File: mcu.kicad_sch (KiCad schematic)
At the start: 7 parts, among them SW1 Reset Switch, U2 STM32F030F4Px

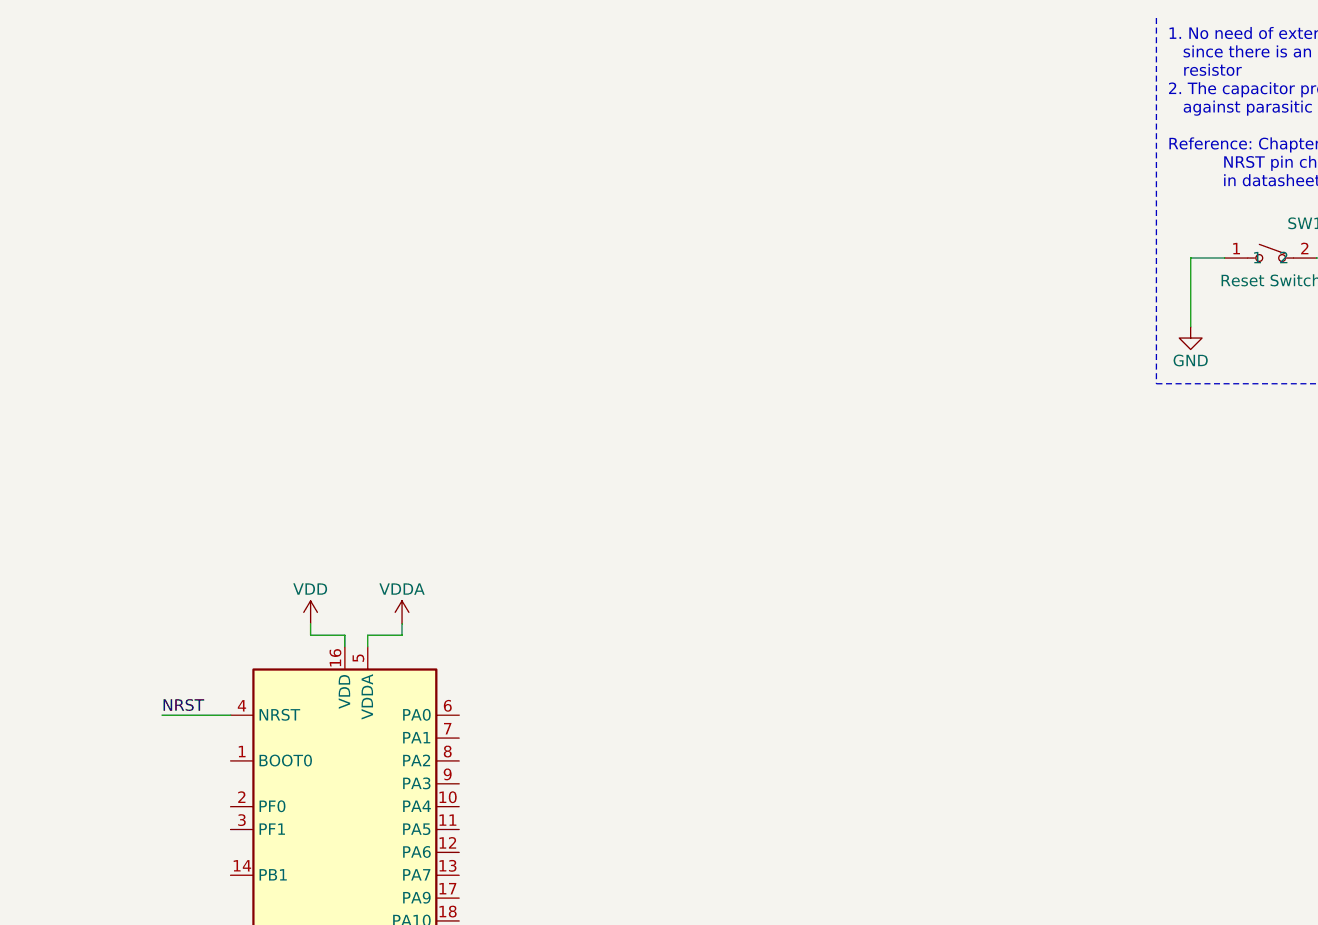
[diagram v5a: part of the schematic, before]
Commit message: feat(boot_mode): Add boot mode selection circuit for MCU BOOT0 pin
Implements the boot mode selection circuitry for the microcontroller's BOOT0 pin in the schematic.

This includes:
- Placement of selection components (e.g., jumper, switch, resistors).
- Configuration to allow selection of different boot modes.
- Connection to the MCU's BOOT0 pin.

This addition provides flexibility in configuring the microcontroller's boot process for tasks such as programming or normal operation.
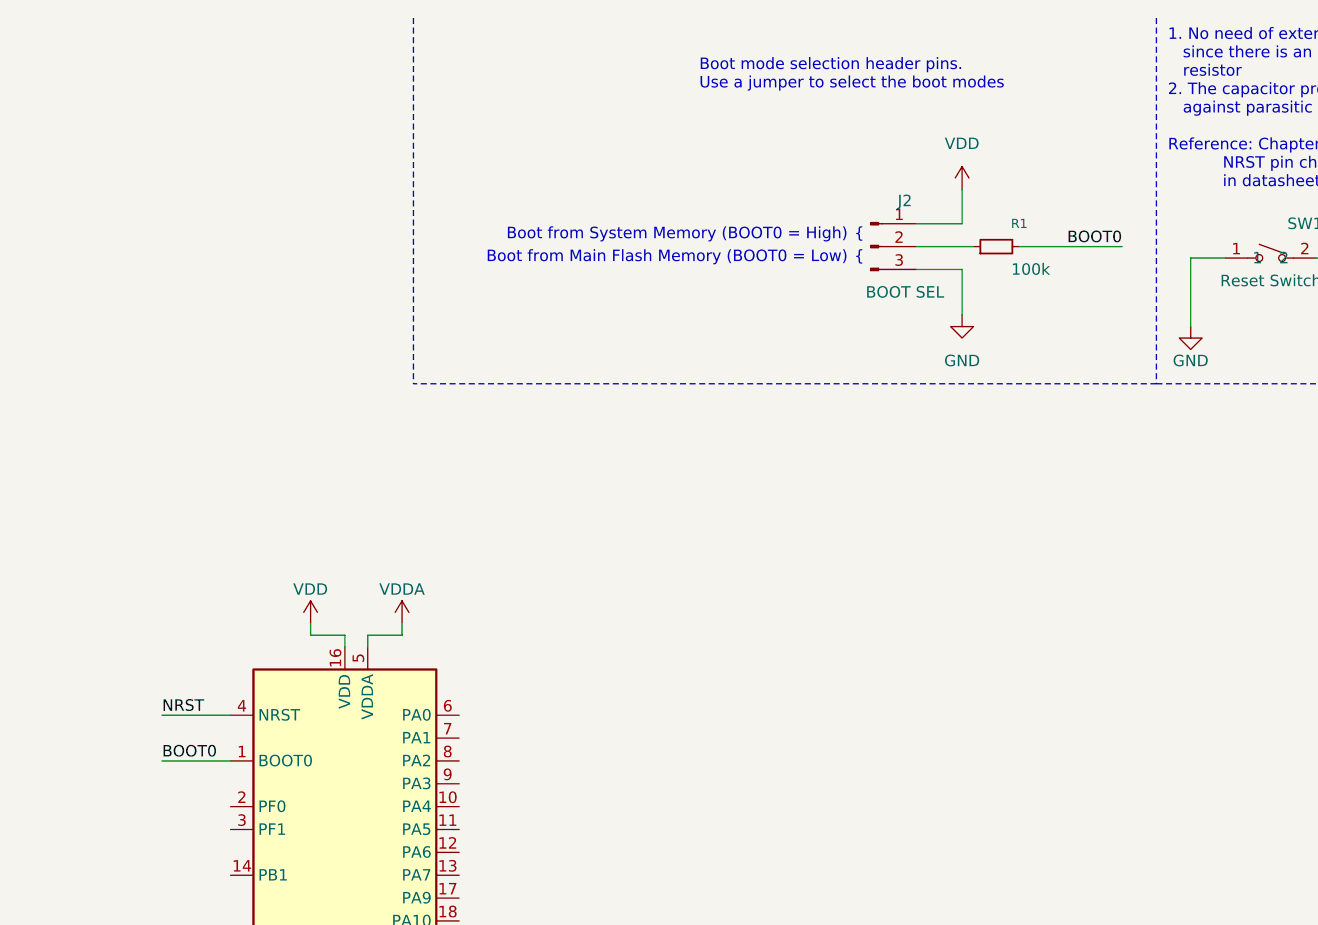
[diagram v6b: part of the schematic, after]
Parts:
- added J2: BOOT SEL, symbol Connector:Conn_01x03_Pin
- added R1: 100k, Resistor_SMD:R_0201_0603Metric_Pad0.64x0.40mm_HandSolder, symbol Device:R_Small
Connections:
- net GND: now also J2.3 (Pin_3)
- net VDD: now also J2.1 (Pin_1)
- net BOOT0: now reaches U2.1 (BOOT0)
- net BOOT0: now also R1.2
- new net: J2.2 (Pin_2), R1.1
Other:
- note added: "Boot from Main Flash Memory (BOOT0 = Low)"
- note added: "Boot from System Memory (BOOT0 = High)"
- note added: "Boot mode selection header pins. Use a jumper to select the boot modes"
- note added: "{"

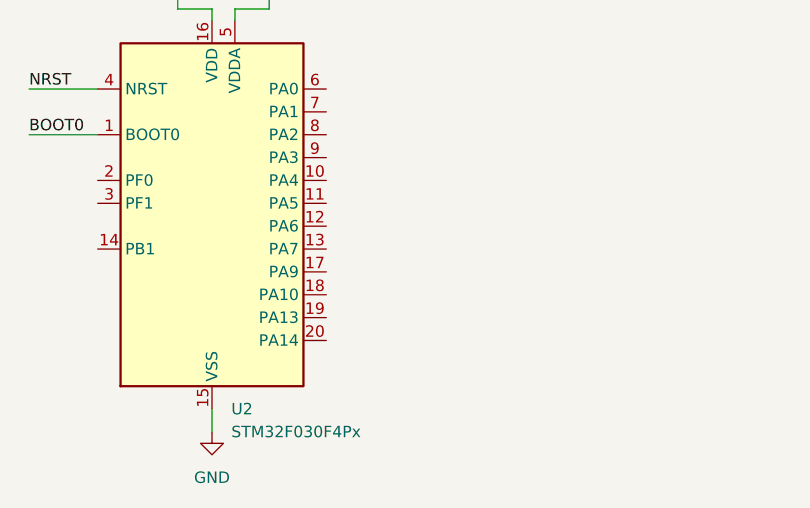
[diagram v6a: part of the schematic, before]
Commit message: feat(usb-uart): add FT232RL USB‑UART bridge and wire RX/TX to MCU
Added the FT232RL USB‑to‑UART interface IC (FT232RL) into the schematic and powered it from the 3.3 V and 5 V rails. Exposed its TTL-level RXD and TXD pins through the hierarchical sheet and connected it to the MCU

- Placed FT232RL SSOP‑28 symbol and footprint, tied VCCIO to 3.3 V, VCC to USB_VCC, and GND to ground.
- Left legacy RS‑232 control lines (DSR#, DCD#, RI#) and CBUS pins unconnected.
- Updated hierarchy:added sheet pins on USB_UART page.

This enables USB‑serial communication between host PC and STM32F030F4Px
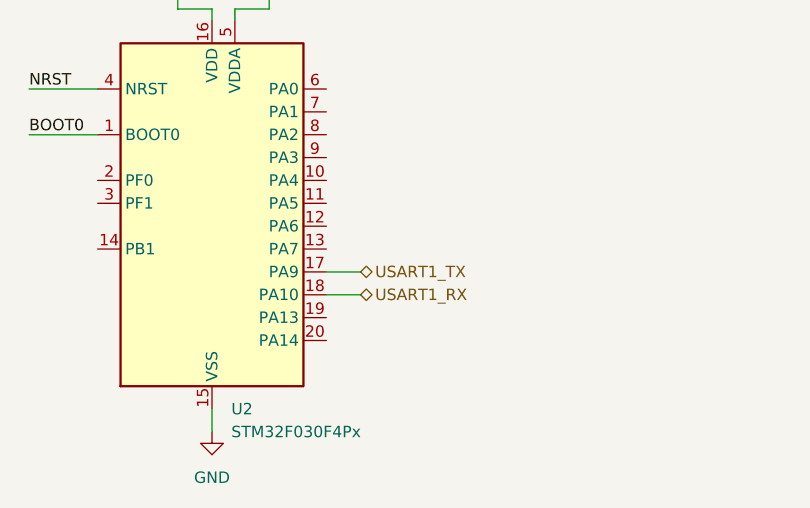
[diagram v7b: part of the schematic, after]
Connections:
- net USART1_TX: now reaches U2.17 (PA9)
- net USART1_RX: now reaches U2.18 (PA10)
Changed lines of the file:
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@@
 		(color 0 0 0 0)
 	)
+	(wire
+		(pts
+			(xy 167.64 110.49) (xy 171.45 110.49)
+		)
+		(stroke
+			(width 0)
+			(type default)
+		)
+	)
 	(polyline
 		(pts
@@
 		(pts
 			(xy 134.62 95.25) (xy 142.24 95.25)
+		)
+		(stroke
+			(width 0)
+			(type default)
+		)
+	)
+	(wire
+		(pts
+			(xy 167.64 113.03) (xy 171.45 113.03)
 		)
 		(stroke
@@
 			)
 			(justify right bottom)
+		)
+	)
+	(hierarchical_label "USART1_TX"
+		(shape bidirectional)
+		(at 171.45 110.49 0)
+		(effects
+			(font
+				(size 1.27 1.27)
+			)
+			(justify left)
 		)
 	)
@@
 		)
 	)
+	(hierarchical_label "USART1_RX"
+		(shape bidirectional)
+		(at 171.45 113.03 0)
+		(effects
+			(font
+				(size 1.27 1.27)
+			)
+			(justify left)
+		)
+	)

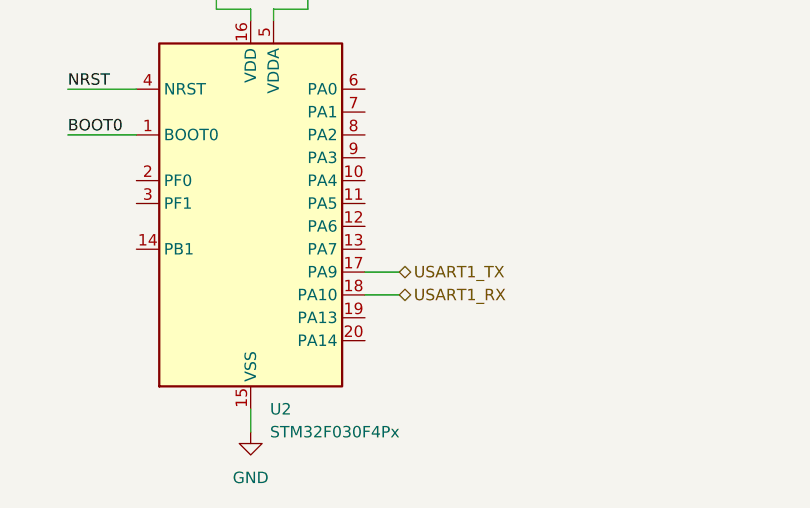
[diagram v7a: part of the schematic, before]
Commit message: fix: Separted CC1 and CC2 resistors and fixed the UART label directions
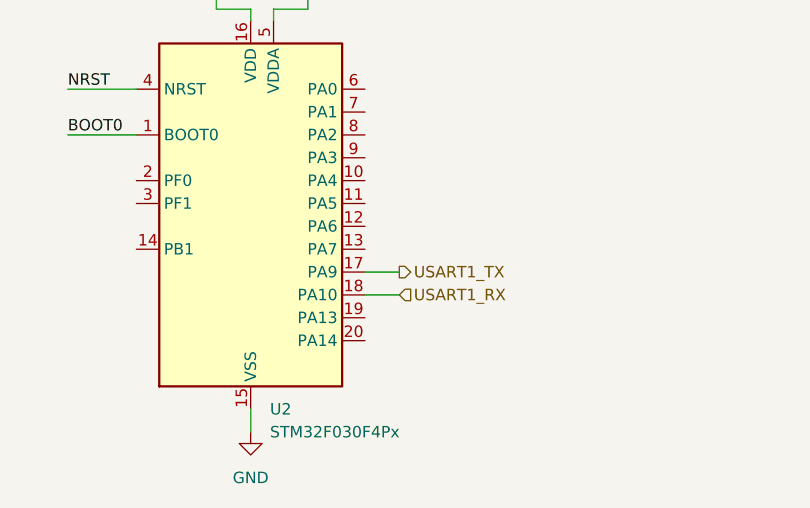
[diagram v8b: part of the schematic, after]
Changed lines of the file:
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@@
 	)
 	(hierarchical_label "USART1_TX"
-		(shape bidirectional)
+		(shape output)
 		(at 171.45 110.49 0)
 		(effects
@@
 	)
 	(hierarchical_label "USART1_RX"
-		(shape bidirectional)
+		(shape input)
 		(at 171.45 113.03 0)
 		(effects
